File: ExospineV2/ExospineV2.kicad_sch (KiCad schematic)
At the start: 1 part, among them U1 RASPBERRY_PI_4B_4GB

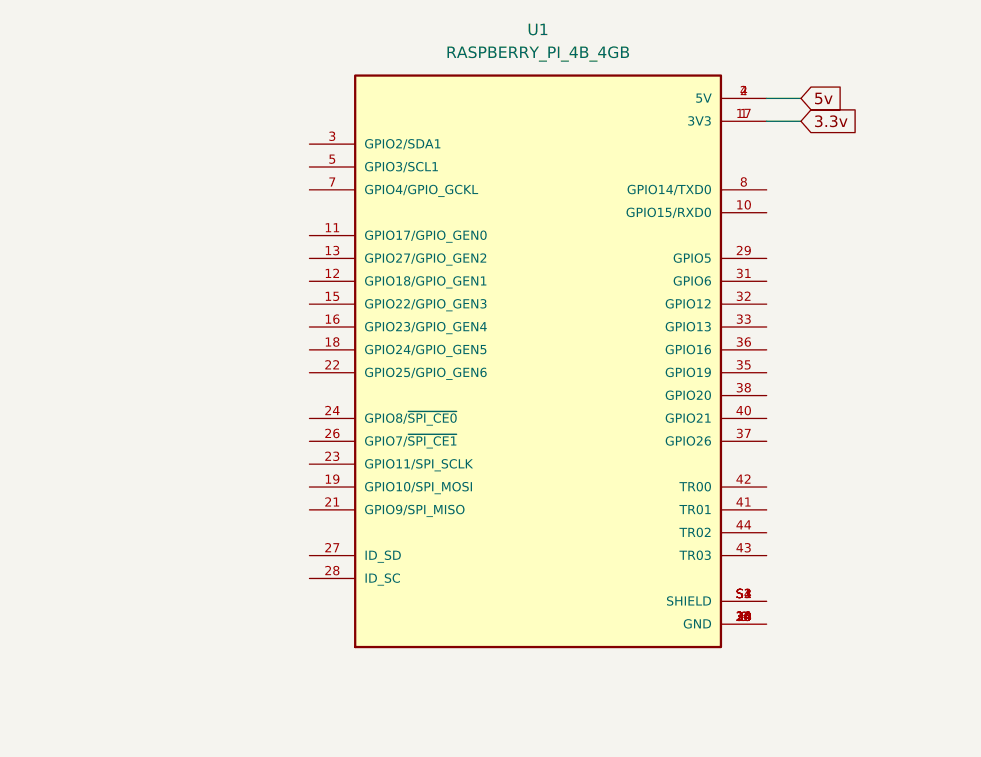
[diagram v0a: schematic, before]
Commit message: Ajout de pin assignment du Raspberry Pi
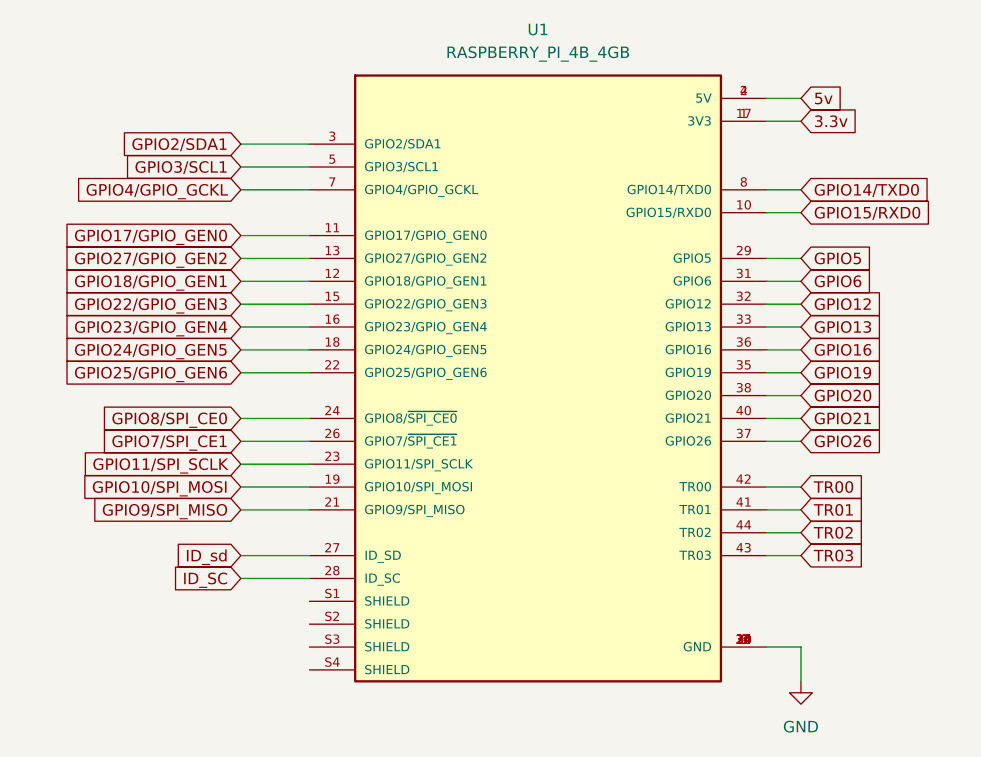
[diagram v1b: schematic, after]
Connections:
- net GPIO15/RXD0: now reaches U1.10 (GPIO15/RXD0)
- net GPIO17/GPIO_GEN0: now reaches U1.11 (GPIO17/GPIO_GEN0)
- net GPIO18/GPIO_GEN1: now reaches U1.12 (GPIO18/GPIO_GEN1)
- net GPIO27/GPIO_GEN2: now reaches U1.13 (GPIO27/GPIO_GEN2)
- net GND: now reaches U1.14 (GND), U1.20 (GND), U1.25 (GND), U1.30 (GND), U1.34 (GND), U1.39 (GND), U1.6 (GND), U1.9 (GND)
- net GPIO22/GPIO_GEN3: now reaches U1.15 (GPIO22/GPIO_GEN3)
- net GPIO23/GPIO_GEN4: now reaches U1.16 (GPIO23/GPIO_GEN4)
- net GPIO24/GPIO_GEN5: now reaches U1.18 (GPIO24/GPIO_GEN5)
- net GPIO10/SPI_MOSI: now reaches U1.19 (GPIO10/SPI_MOSI)
- net GPIO9/SPI_MISO: now reaches U1.21 (GPIO9/SPI_MISO)
- net GPIO25/GPIO_GEN6: now reaches U1.22 (GPIO25/GPIO_GEN6)
- net GPIO11/SPI_SCLK: now reaches U1.23 (GPIO11/SPI_SCLK)
- net GPIO8/SPI_CE0: now reaches U1.24 (GPIO8/~{SPI_CE0})
- net GPIO7/SPI_CE1: now reaches U1.26 (GPIO7/~{SPI_CE1})
- net ID_sd: now reaches U1.27 (ID_SD)
- net ID_SC: now reaches U1.28 (ID_SC)
- net GPIO5: now reaches U1.29 (GPIO5)
- net GPIO2/SDA1: now reaches U1.3 (GPIO2/SDA1)
- net GPIO6: now reaches U1.31 (GPIO6)
- net GPIO12: now reaches U1.32 (GPIO12)
- net GPIO13: now reaches U1.33 (GPIO13)
- net GPIO19: now reaches U1.35 (GPIO19)
- net GPIO16: now reaches U1.36 (GPIO16)
- net GPIO26: now reaches U1.37 (GPIO26)
- net GPIO20: now reaches U1.38 (GPIO20)
- net GPIO21: now reaches U1.40 (GPIO21)
- net TR01: now reaches U1.41 (TR01)
- net TR00: now reaches U1.42 (TR00)
- net TR03: now reaches U1.43 (TR03)
- net TR02: now reaches U1.44 (TR02)
- net GPIO3/SCL1: now reaches U1.5 (GPIO3/SCL1)
- net GPIO4/GPIO_GCKL: now reaches U1.7 (GPIO4/GPIO_GCKL)
- net GPIO14/TXD0: now reaches U1.8 (GPIO14/TXD0)
- now unconnected: U1.S1 (SHIELD), U1.S2 (SHIELD), U1.S3 (SHIELD), U1.S4 (SHIELD)
